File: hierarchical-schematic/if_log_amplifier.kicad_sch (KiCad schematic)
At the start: 79 parts, among them J301 Coax, J302 SMA Panel Mount, J303 SMA Panel Mount, J304 SMA Panel Mount, J305 Conn_01x03, J306 Conn_01x02, J307 Conn_Coaxial, Q301 2N3904, T301 FT37-43 8:2 t, U301 AD603AQ, U302 L78L05_TO92, U303 LM317L_TO92, U304 ${SIM.PARAMS}, U305 CA3140

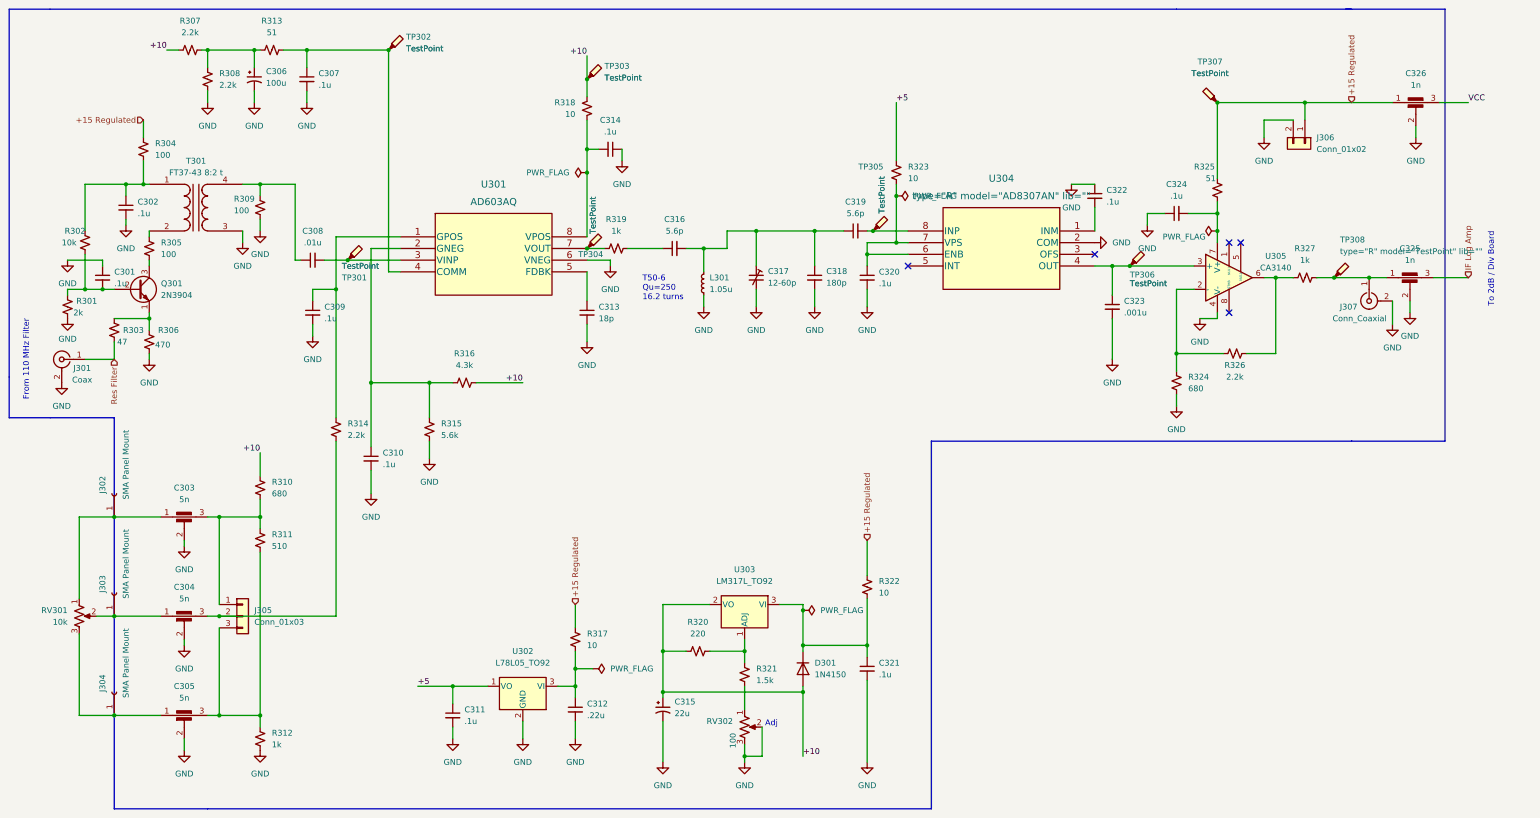
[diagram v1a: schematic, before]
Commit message: erc changes for hierarchical schematic
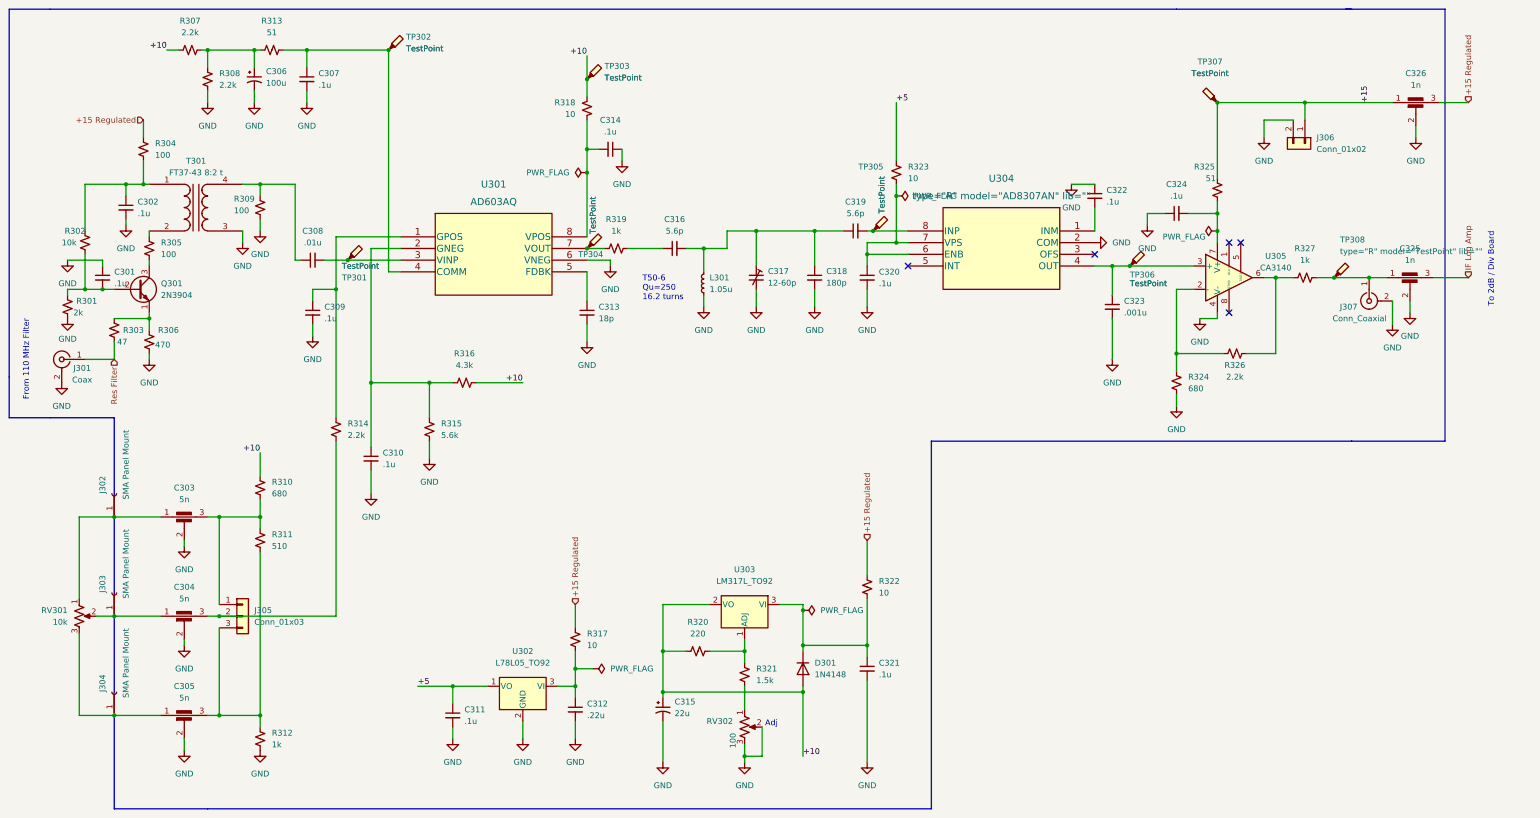
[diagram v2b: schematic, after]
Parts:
- D301: value 1N4150 -> 1N4148; symbol Diode:1N4152 -> Diode:1N4148
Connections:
- net VCC is gone; now on net +15 Regulated: C326.3
- net +15 Regulated: no longer C326.1, J306.1 (Pin_1), R325.2, TP307.1
- new net +15: C326.1, J306.1 (Pin_1), R325.2, TP307.1
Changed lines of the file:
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@@
-    (effects (font (size 1.27 1.27)) (justify left bottom))
-  )
-  (label "VCC" (at 332.74 34.29 0) (fields_autoplaced)
     (effects (font (size 1.27 1.27)) (justify left bottom))
   )
@@
     (effects (font (size 1.27 1.27)) (justify right bottom))
   )
+  (label "+15" (at 311.15 34.29 90) (fields_autoplaced)
+    (effects (font (size 1.27 1.27)) (justify left bottom))
+  )
   (label "+10" (at 69.85 110.49 180) (fields_autoplaced)
     (effects (font (size 1.27 1.27)) (justify right bottom))
@@
     (effects (font (size 1.27 1.27)) (justify left bottom))
   )
+  (hierarchical_label "+15 Regulated" (shape input) (at 332.74 34.29 90) (fields_autoplaced)
+    (effects (font (size 1.27 1.27)) (justify left))
+  )
   (hierarchical_label "+15 Regulated" (shape input) (at 44.45 38.1 180) (fields_autoplaced)
     (effects (font (size 1.27 1.27)) (justify right))
-  )
-  (hierarchical_label "+15 Regulated" (shape input) (at 307.34 34.29 90) (fields_autoplaced)
-    (effects (font (size 1.27 1.27)) (justify left))
   )
   (hierarchical_label "Res Filter" (shape input) (at 38.1 90.17 270) (fields_autoplaced)
@@
       (effects (font (size 1.27 1.27)) hide)
     )
-    (property "Datasheet" "" (at 311.15 77.47 0)
-      (effects (font (size 1.27 1.27)) hide)
-    )
-    (property "Sim.Enable" "0" (at 311.15 77.47 0)
-      (effects (font (size 1.27 1.27)) hide)
-    )
-    (property "Sim.Device" "SPICE" (at 311.15 77.47 0)
-      (effects (font (size 1.27 1.27)) hide)
-    )
-    (property "Sim.Params" "type=\"J\" model=\"Conn_Coaxial\" lib=\"\"" (at 0 0 0)
-      (effects (font (size 0 0)) hide)
-    )
-    (property "Sim.Pins" "1=1 2=2" (at 0 0 0)
-      (effects (font (size 0 0)) hide)
+    (property "Datasheet" " ~" (at 311.15 77.47 0)
+      (effects (font (size 1.27 1.27)) hide)
     )
     (pin "1")
@@
     )
   )
-  (symbol (lib_id "Diode:1N4152") (at 187.96 157.48 270) (unit 1)
-    (in_bom yes) (on_board yes) (dnp no) (fields_autoplaced)
-    (property "Reference" "D301" (at 190.5 156.2099 90)
-      (effects (font (size 1.27 1.27)) (justify left))
-    )
-    (property "Value" "1N4150" (at 190.5 158.7499 90)
-      (effects (font (size 1.27 1.27)) (justify left))
-    )
-    (property "Footprint" "Diode_THT:D_DO-35_SOD27_P7.62mm_Horizontal" (at 183.515 157.48 0)
-      (effects (font (size 1.27 1.27)) hide)
-    )
-    (property "Datasheet" "https://www.digikey.com/en/products/detail/microchip-technology/1N4150-1/4377992" (at 187.96 157.48 0)
-      (effects (font (size 1.27 1.27)) hide)
-    )
-    (property "Sim.Device" "SPICE" (at 187.96 157.48 0)
+  (symbol (lib_id "Diode:1N4148") (at 187.96 157.48 270) (unit 1)
+    (in_bom yes) (on_board yes) (dnp no) (fields_autoplaced)
+    (property "Reference" "D301" (at 190.5 156.21 90)
+      (effects (font (size 1.27 1.27)) (justify left))
+    )
+    (property "Value" "1N4148" (at 190.5 158.75 90)
+      (effects (font (size 1.27 1.27)) (justify left))
+    )
+    (property "Footprint" "Diode_THT:D_DO-35_SOD27_P7.62mm_Horizontal" (at 187.96 157.48 0)
+      (effects (font (size 1.27 1.27)) hide)
+    )
+    (property "Datasheet" "https://assets.nexperia.com/documents/data-sheet/1N4148_1N4448.pdf" (at 187.96 157.48 0)
+      (effects (font (size 1.27 1.27)) hide)
+    )
+    (property "Sim.Device" "D" (at 187.96 157.48 0)
       (effects (font (size 1.27 1.27)) hide)
     )
@@
       (effects (font (size 0 0)) hide)
     )
-    (property "Sim.Pins" "2=1 1=2" (at 187.96 157.48 0)
+    (property "Sim.Pins" "1=K 2=A" (at 187.96 157.48 0)
       (effects (font (size 1.27 1.27)) hide)
     )
@@
       (effects (font (size 1.27 1.27)) hide)
     )
-    (property "Datasheet" "" (at 26.67 90.17 0)
-      (effects (font (size 1.27 1.27)) hide)
-    )
-    (property "Sim.Enable" "0" (at 26.67 90.17 0)
-      (effects (font (size 1.27 1.27)) hide)
-    )
-    (property "Sim.Device" "SPICE" (at 26.67 90.17 0)
-      (effects (font (size 1.27 1.27)) hide)
-    )
-    (property "Sim.Params" "type=\"J\" model=\"Conn_Coaxial\" lib=\"\"" (at 0 0 0)
-      (effects (font (size 0 0)) hide)
-    )
-    (property "Sim.Pins" "1=1 2=2" (at 0 0 0)
-      (effects (font (size 0 0)) hide)
-    )
-    (pin "1")
+    (property "Datasheet" " ~" (at 26.67 90.17 0)
+      (effects (font (size 1.27 1.27)) hide)
+    )
+    (pin "1")

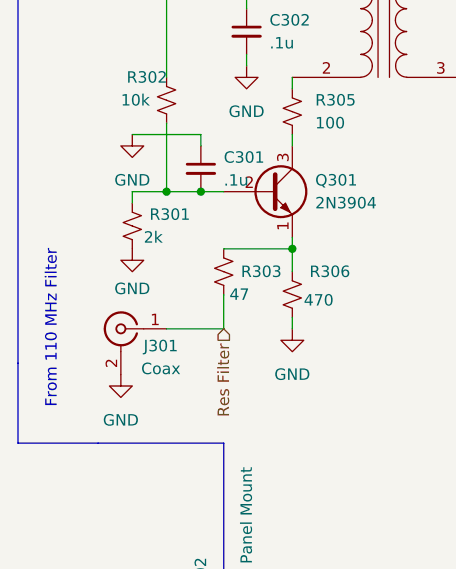
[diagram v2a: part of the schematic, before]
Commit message: correction to hierarchical schematic
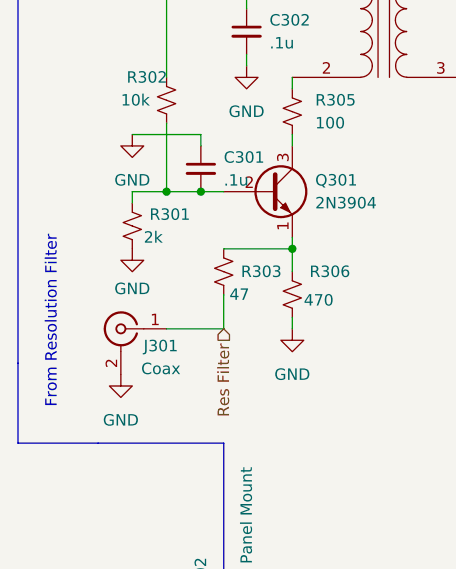
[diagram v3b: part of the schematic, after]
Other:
- note added: "From Resolution Filter"
- note removed: "From 110 MHz Filter"
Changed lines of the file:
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@@
     (effects (font (size 1.27 1.27)) (justify left bottom))
   )
-  (text "From 110 MHz Filter" (at 19.685 99.06 90)
+  (text "From Resolution Filter" (at 19.685 99.06 90)
     (effects (font (size 1.27 1.27)) (justify left bottom))
   )
